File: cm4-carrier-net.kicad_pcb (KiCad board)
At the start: 4 copper layers, 91.4 x 40.5 mm, 69 parts, among them J1 USB_C_Receptacle_USB2.0, J2 Micro_SD_Card, J3 Abracon_ARJM11-502, J4 20021121-00010C4LF, J5 block, J6 USB_A, Q1 DMP2066LSN, Q2 FDMT800152DC, Q3 FDMT800152DC, SW1 BOOT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

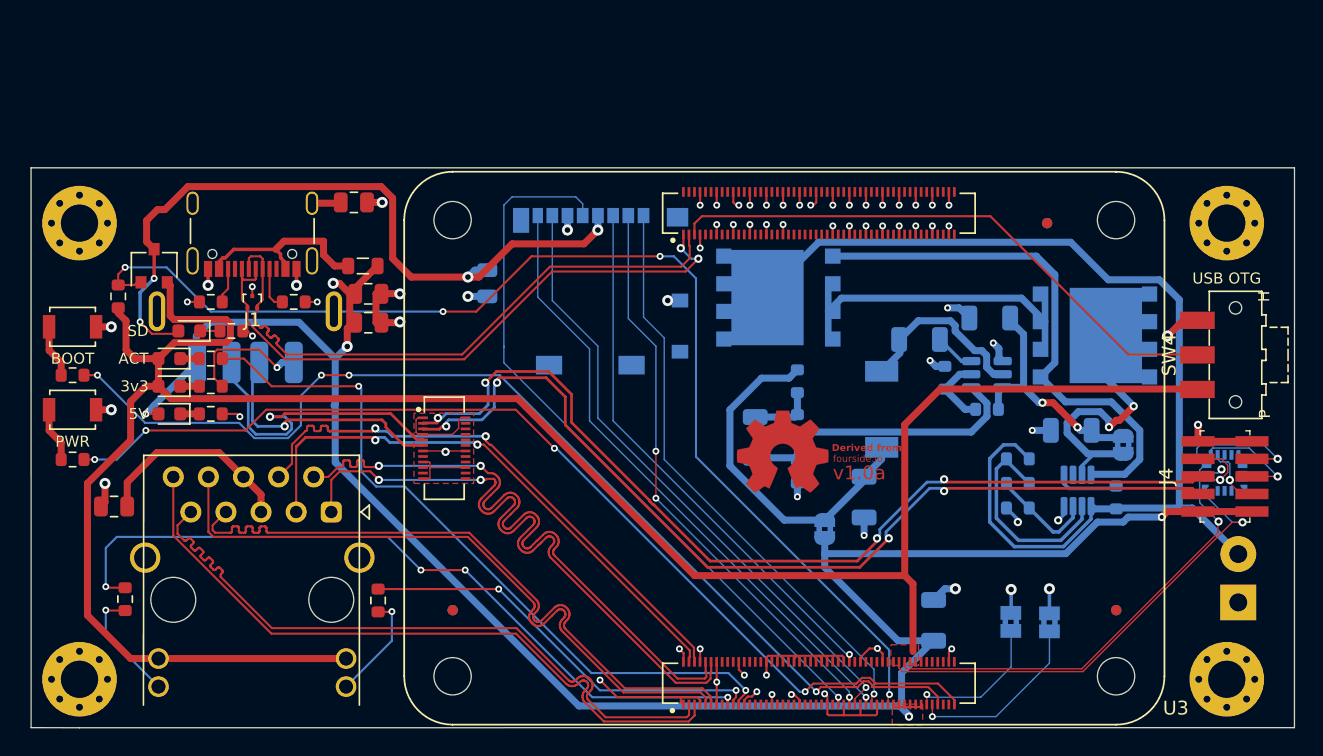
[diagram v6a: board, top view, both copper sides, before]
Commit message: added camera zif connector
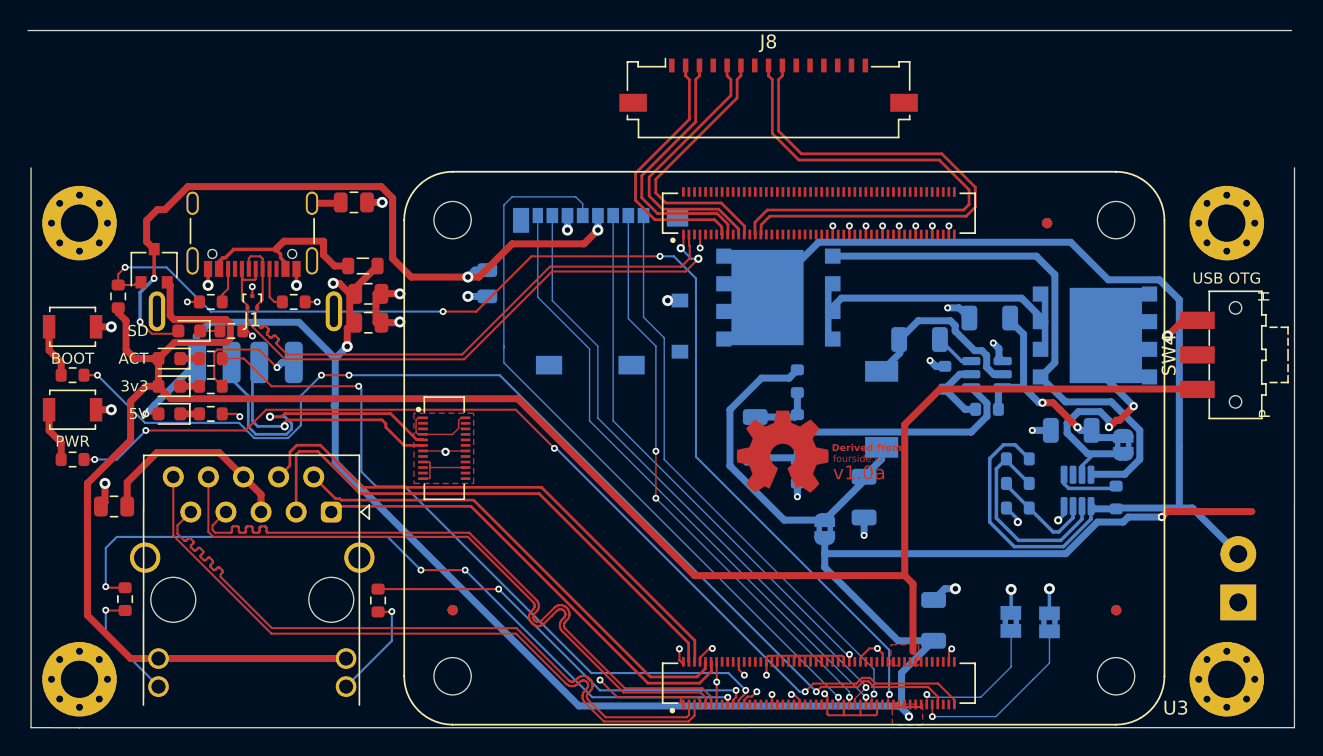
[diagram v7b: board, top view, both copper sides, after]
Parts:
- removed J4: 20021121-00010C4LF, digikey-footprints:PinHeader_2x5_P1.27mm
- removed U4: STM32C011J4Mx, Package_DFN_QFN:ST_UFQFPN-20_3x3mm_P0.5mm
- added J8: Conn_01x15_MountingPin, Connector_FFC-FPC:Molex_200528-0150_1x15-1MP_P1.00mm_Horizontal, F.Cu at (133.3, 87.0)
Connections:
- U3 pad JP1_97: unconnected-(U3A-CAMERA_PDN_L-PadJP1_97) -> /CAMERA_PDN
- U3 pad JP2_15: unconnected-(U3B-MIPI_CSI_RX0_D0N-PadJP2_15) -> /MIPI_CSI_RX0_D0N
- U3 pad JP2_17: unconnected-(U3B-MIPI_CSI_RX0_D0P-PadJP2_17) -> /MIPI_CSI_RX0_D0P
- U3 pad JP2_21: unconnected-(U3B-MIPI_CSI_RX0_D1N-PadJP2_21) -> /MIPI_CSI_RX1_D0N
- U3 pad JP2_23: unconnected-(U3B-MIPI_CSI_RX0_D1P-PadJP2_23) -> /MIPI_CSI_RX1_D0P
- U3 pad JP2_27: unconnected-(U3B-MIPI_CSI_RX_CLK0N-PadJP2_27) -> /MIPI_CSI_RX_CLK0N
- U3 pad JP2_29: unconnected-(U3B-MIPI_CSI_RX_CLK0P-PadJP2_29) -> /MIPI_CSI_RX_CLK0P
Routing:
- net /USB1-: track 69.0 -> 0.00 mm, vias 4 -> 0
- net /USB1+: track 69.0 -> 0.00 mm, vias 4 -> 0
- net /USB_OTG_ID: track 40.9 -> 0.00 mm
- net /MIPI_CSI_RX_CLK0N: track 0.00 -> 38.9 mm
- net /MIPI_CSI_RX_CLK0P: track 0.00 -> 38.9 mm
- net /I2C1_SCL-: track 34.0 -> 0.00 mm, vias 1 -> 0
- net /I2C1_SDA+: track 32.8 -> 0.00 mm, vias 1 -> 0
- net GND: track 132.1 -> 109.7 mm, vias 74 -> 51
- net /MIPI_CSI_RX1_D0N: track 0.00 -> 19.9 mm
- net /MIPI_CSI_RX1_D0P: track 0.00 -> 19.8 mm
- net /MIPI_CSI_RX0_D0P: track 0.00 -> 19.1 mm
- net /MIPI_CSI_RX0_D0N: track 0.00 -> 19.1 mm
- net /E0_TR0+: track 49.9 -> 34.0 mm, vias 2 -> 0
- net /E0_TR0-: track 49.9 -> 35.1 mm, vias 2 -> 0
- net /I2C_TO_DB_SDA: track 9.37 -> 0.00 mm, vias 1 -> 0
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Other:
- board size 91.4 x 40.5 mm -> 91.6 x 50.4 mm

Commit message: tuned length of traces and pairs
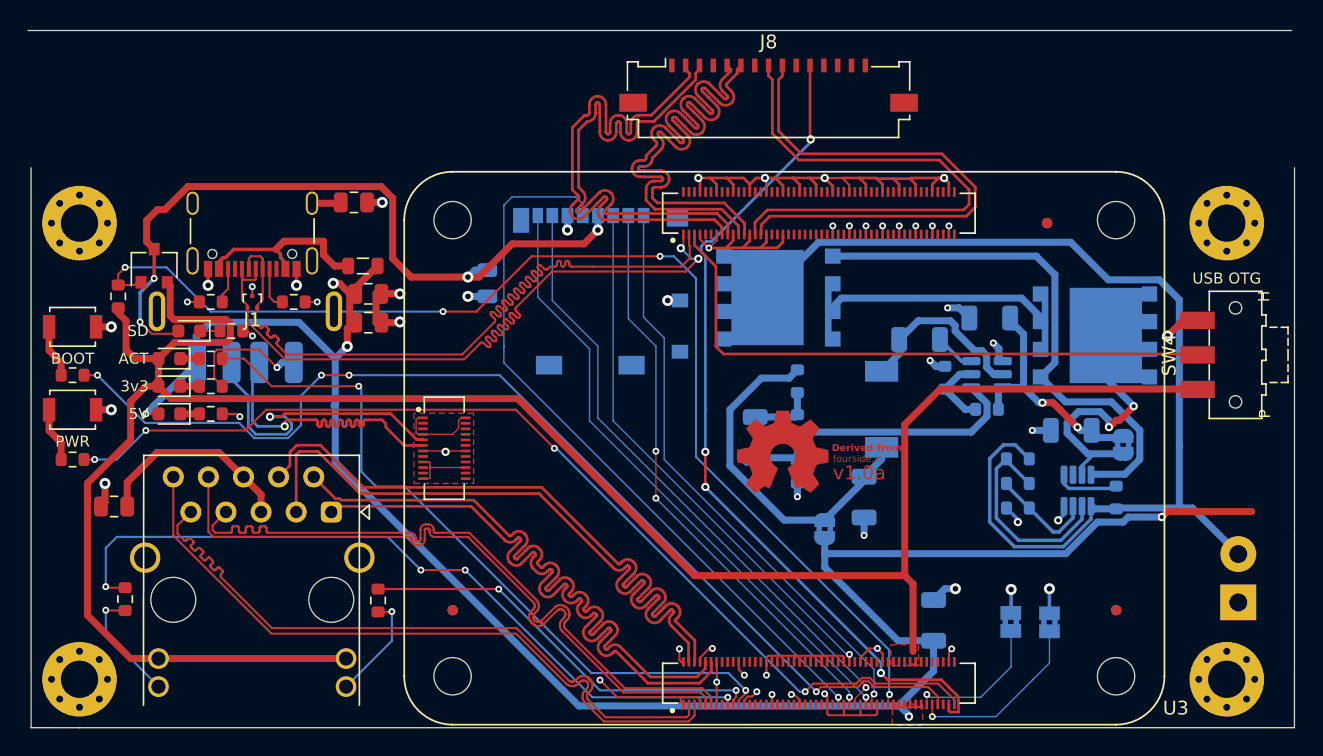
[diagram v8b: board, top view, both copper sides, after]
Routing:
- net /CAMERA_PDN: track 0.00 -> 61.5 mm, vias 0 -> 4
- net GND: track 109.7 -> 157.0 mm, vias 51 -> 55
- net /USB_OTG_ID: track 0.00 -> 43.8 mm
- net /MIPI_CSI_RX0_D0P: track 19.1 -> 38.8 mm
- net /MIPI_CSI_RX0_D0N: track 19.1 -> 38.8 mm
- net /MIPI_CSI_RX1_D0P: track 19.8 -> 38.6 mm
- net /MIPI_CSI_RX1_D0N: track 19.9 -> 38.6 mm
- net /E0_TR0+: track 34.0 -> 48.7 mm
- net /E0_TR0-: track 35.1 -> 49.7 mm
- net /USB_D-: track 44.5 -> 55.3 mm
- net /E0_TR1-: track 39.0 -> 48.9 mm
- net /E0_TR1+: track 39.7 -> 49.6 mm
- net /USB_D+: track 45.2 -> 51.6 mm
- net /USB+: track 18.2 -> 22.5 mm
- net /E0_TR2+: track 49.0 -> 50.7 mm
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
